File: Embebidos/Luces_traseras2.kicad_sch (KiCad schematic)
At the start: 9 parts, among them J4 RJ45, J5 RJ45, Q1 Q_PMOS_Leds5v, Q2 Q_PMOS_Infrarrojo

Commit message: anotaciones_fix
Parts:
- renumbered J5 to J8, J4 to J9, JT3 to JT1, JT1 to JT2, JT2 to JT3, Q1 to Q4, Q2 to Q5, R2 to R24, R1 to R25
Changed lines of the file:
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@@
   (symbol (lib_id "Connector:RJ45") (at 168.91 93.98 0) (unit 1)
     (in_bom yes) (on_board yes)
-    (property "Reference" "J4" (id 0) (at 170.3578 77.0382 0))
+    (property "Reference" "J9" (id 0) (at 170.3578 77.0382 0))
     (property "Value" "RJ45" (id 1) (at 170.3578 79.3496 0))
     (property "Footprint" "" (id 2) (at 168.91 93.345 90)
@@
   (symbol (lib_id "Connector:Conn_01x03_Male") (at 241.3 64.77 180) (unit 1)
     (in_bom yes) (on_board yes)
-    (property "Reference" "JT1" (id 0) (at 238.5568 71.9074 0))
+    (property "Reference" "JT2" (id 0) (at 238.5568 71.9074 0))
     (property "Value" "8 LEDS RGB Izquierda" (id 1) (at 238.5568 69.596 0))
     (property "Footprint" "" (id 2) (at 241.3 64.77 0)
@@
   (symbol (lib_id "Connector:Conn_01x03_Male") (at 241.3 90.17 180) (unit 1)
     (in_bom yes) (on_board yes)
-    (property "Reference" "JT2" (id 0) (at 238.5568 97.3074 0))
+    (property "Reference" "JT3" (id 0) (at 238.5568 97.3074 0))
     (property "Value" "INFRARROJO SHARP" (id 1) (at 238.5568 94.996 0))
     (property "Footprint" "" (id 2) (at 241.3 90.17 0)
@@
   (symbol (lib_id "Connector:Conn_01x03_Male") (at 240.03 114.3 180) (unit 1)
     (in_bom yes) (on_board yes)
-    (property "Reference" "JT3" (id 0) (at 237.2868 121.4374 0))
+    (property "Reference" "JT1" (id 0) (at 237.2868 121.4374 0))
     (property "Value" "8 LEDS RGB Derecha" (id 1) (at 237.2868 119.126 0))
     (property "Footprint" "" (id 2) (at 240.03 114.3 0)
@@
   (symbol (lib_id "Device:R") (at 203.2 76.2 270) (unit 1)
     (in_bom yes) (on_board yes)
-    (property "Reference" "R1" (id 0) (at 203.2 70.9422 90))
+    (property "Reference" "R25" (id 0) (at 203.2 70.9422 90))
     (property "Value" "470" (id 1) (at 203.2 73.2536 90))
     (property "Footprint" "" (id 2) (at 203.2 74.422 90)
@@
   (symbol (lib_id "Device:R") (at 201.93 107.95 270) (unit 1)
     (in_bom yes) (on_board yes)
-    (property "Reference" "R2" (id 0) (at 201.93 102.6922 90))
+    (property "Reference" "R24" (id 0) (at 201.93 102.6922 90))
     (property "Value" "470" (id 1) (at 201.93 105.0036 90))
     (property "Footprint" "" (id 2) (at 201.93 106.172 90)
@@
   (symbol (lib_id "Connector:RJ45") (at 111.76 91.44 180) (unit 1)
     (in_bom yes) (on_board yes)
-    (property "Reference" "J5" (id 0) (at 120.142 91.5416 0)
+    (property "Reference" "J8" (id 0) (at 120.142 91.5416 0)
       (effects (font (size 1.27 1.27)) (justify right))
     )
@@
   (symbol (lib_id "Device:Q_PMOS_GSD") (at 50.8 116.84 0) (unit 1)
     (in_bom yes) (on_board yes)
-    (property "Reference" "Q1" (id 0) (at 55.9816 115.6716 0)
+    (property "Reference" "Q4" (id 0) (at 55.9816 115.6716 0)
       (effects (font (size 1.27 1.27)) (justify left))
     )
@@
   (symbol (lib_id "Device:Q_PMOS_GSD") (at 62.23 109.22 0) (unit 1)
     (in_bom yes) (on_board yes)
-    (property "Reference" "Q2" (id 0) (at 67.4116 108.0516 0)
+    (property "Reference" "Q5" (id 0) (at 67.4116 108.0516 0)
       (effects (font (size 1.27 1.27)) (justify left))
     )
@@
   (symbol (lib_id "power:+5V") (at 53.34 127 180) (unit 1)
     (in_bom yes) (on_board yes) (fields_autoplaced)
-    (property "Reference" "#PWR?" (id 0) (at 53.34 123.19 0)
+    (property "Reference" "#PWR038" (id 0) (at 53.34 123.19 0)
       (effects (font (size 1.27 1.27)) hide)
     )
@@
   (symbol (lib_id "power:GND") (at 27.94 91.44 270) (unit 1)
     (in_bom yes) (on_board yes) (fields_autoplaced)
-    (property "Reference" "#PWR?" (id 0) (at 21.59 91.44 0)
+    (property "Reference" "#PWR037" (id 0) (at 21.59 91.44 0)
       (effects (font (size 1.27 1.27)) hide)
     )

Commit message: Mosfet Luces
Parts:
- removed Q4: Q_PMOS_Leds5v, symbol Device:Q_PMOS_GSD
- removed Q5: Q_PMOS_Infrarrojo, symbol Device:Q_PMOS_GSD
- added IC?: DMP3056LSD-13, SOIC127P600X175-8N, symbol DMP3056LSD-13:DMP3056LSD-13
- added R? (x2): 1k, symbol Device:R
- added R? (x2): 100k, symbol Device:R
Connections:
- net +5V: now also IC?.1 (S1), IC?.3 (S2), R?.2, R?.2
- net ctr 5v inf: now also R?.1, R?.1
- net ctr 5v leds: now also R?.1, R?.1
- net at J8.2: now also IC?.8 (D1_2)
- net at J8.3: now also IC?.5 (D2_1)
- new net: IC?.2 (G1), R?.2
- new net: IC?.4 (G2), R?.2
- no-connect marks 4 -> 6

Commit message: se agrego el bonito
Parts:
- gave numbers to parts that had none: 5
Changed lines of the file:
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@@
   (symbol (lib_id "Device:R") (at 49.53 137.16 90) (unit 1)
     (in_bom yes) (on_board yes)
-    (property "Reference" "R?" (id 0) (at 49.53 134.62 90))
+    (property "Reference" "R28" (id 0) (at 49.53 134.62 90))
     (property "Value" "1k" (id 1) (at 49.53 137.16 90))
     (property "Footprint" "" (id 2) (at 49.53 138.938 90)
@@
   (symbol (lib_id "Device:R") (at 46.99 115.57 180) (unit 1)
     (in_bom yes) (on_board yes)
-    (property "Reference" "R?" (id 0) (at 44.45 115.57 90))
+    (property "Reference" "R27" (id 0) (at 44.45 115.57 90))
     (property "Value" "100k" (id 1) (at 46.99 115.57 90))
     (property "Footprint" "" (id 2) (at 48.768 115.57 90)
@@
   (symbol (lib_id "power:+5V") (at 46.99 109.22 0) (unit 1)
     (in_bom yes) (on_board yes)
-    (property "Reference" "#PWR?" (id 0) (at 46.99 113.03 0)
+    (property "Reference" "#PWR0104" (id 0) (at 46.99 113.03 0)
       (effects (font (size 1.27 1.27)) hide)
     )
@@
   (symbol (lib_id "Device:R") (at 50.8 127 90) (unit 1)
     (in_bom yes) (on_board yes)
-    (property "Reference" "R?" (id 0) (at 50.8 124.46 90))
+    (property "Reference" "R29" (id 0) (at 50.8 124.46 90))
     (property "Value" "1k" (id 1) (at 50.8 127 90))
     (property "Footprint" "" (id 2) (at 50.8 128.778 90)
@@
   (symbol (lib_id "Device:R") (at 35.56 132.08 180) (unit 1)
     (in_bom yes) (on_board yes)
-    (property "Reference" "R?" (id 0) (at 33.02 132.08 90))
+    (property "Reference" "R26" (id 0) (at 33.02 132.08 90))
     (property "Value" "100k" (id 1) (at 35.56 132.08 90))
     (property "Footprint" "" (id 2) (at 37.338 132.08 90)
@@
   (symbol (lib_id "DMP3056LSD-13:DMP3056LSD-13") (at 57.15 124.46 90) (unit 1)
     (in_bom yes) (on_board yes) (fields_autoplaced)
-    (property "Reference" "IC?" (id 0) (at 68.58 110.4899 90)
+    (property "Reference" "IC2" (id 0) (at 68.58 110.4899 90)
       (effects (font (size 1.27 1.27)) (justify right))
     )
@@
   (symbol (lib_id "power:+5V") (at 35.56 125.73 0) (unit 1)
     (in_bom yes) (on_board yes)
-    (property "Reference" "#PWR?" (id 0) (at 35.56 129.54 0)
+    (property "Reference" "#PWR0105" (id 0) (at 35.56 129.54 0)
       (effects (font (size 1.27 1.27)) hide)
     )

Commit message: transistores traseros
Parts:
- removed IC2: DMP3056LSD-13, SOIC127P600X175-8N, symbol DMP3056LSD-13:DMP3056LSD-13
- removed J9: RJ45, symbol Connector:RJ45
- removed JT1: 8 LEDS RGB Derecha, symbol Connector:Conn_01x03_Male
- removed JT2: 8 LEDS RGB Izquierda, symbol Connector:Conn_01x03_Male
- removed JT3: INFRARROJO SHARP, symbol Connector:Conn_01x03_Male
- removed R26: 100k, symbol Device:R
- removed R29: 1k, symbol Device:R
- added Q?: BSS138, Package_TO_SOT_SMD:SOT-23, symbol Transistor_FET:BSS138
- added Q? (x2): DMP3056LSDQ-13, DMP3056LSD:SOIC127P600X175-8N, symbol DMP3056LSDQ-13:DMP3056LSDQ-13
- added R?: 100k, symbol Device:R
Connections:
- net ctr 5v inf is gone; now on net GND: R27.1
- net +5V: now also Q?.1, Q?.3, R?.2; no longer R27.2
- net Din_der: now also R25.2; no longer J8.1
- net Din_izq: now also R24.2; no longer J8.6
- net GND: now also Q?.2 (S)
- net at R25.1: now also J8.1
- net at R24.1: now also J8.6
- net VCC_LEDS: now reaches J8.2
- net VCC_LEDS: now also Q?.7, Q?.8
- net VCC_INF: now reaches J8.3
- net VCC_INF: now also Q?.5, Q?.6
- net at R28.2: now also R27.2, Q?.1 (G)
- net ctr 5v leds renamed ctr_trasero
- new net: Q?.2, Q?.3 (D), Q?.4, R?.1
- no-connect marks 6 -> 2
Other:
- note added: "2. Control Vcc leds 3. Control Vcc inf"
- moved on the sheet: R24, R25, R27, R28

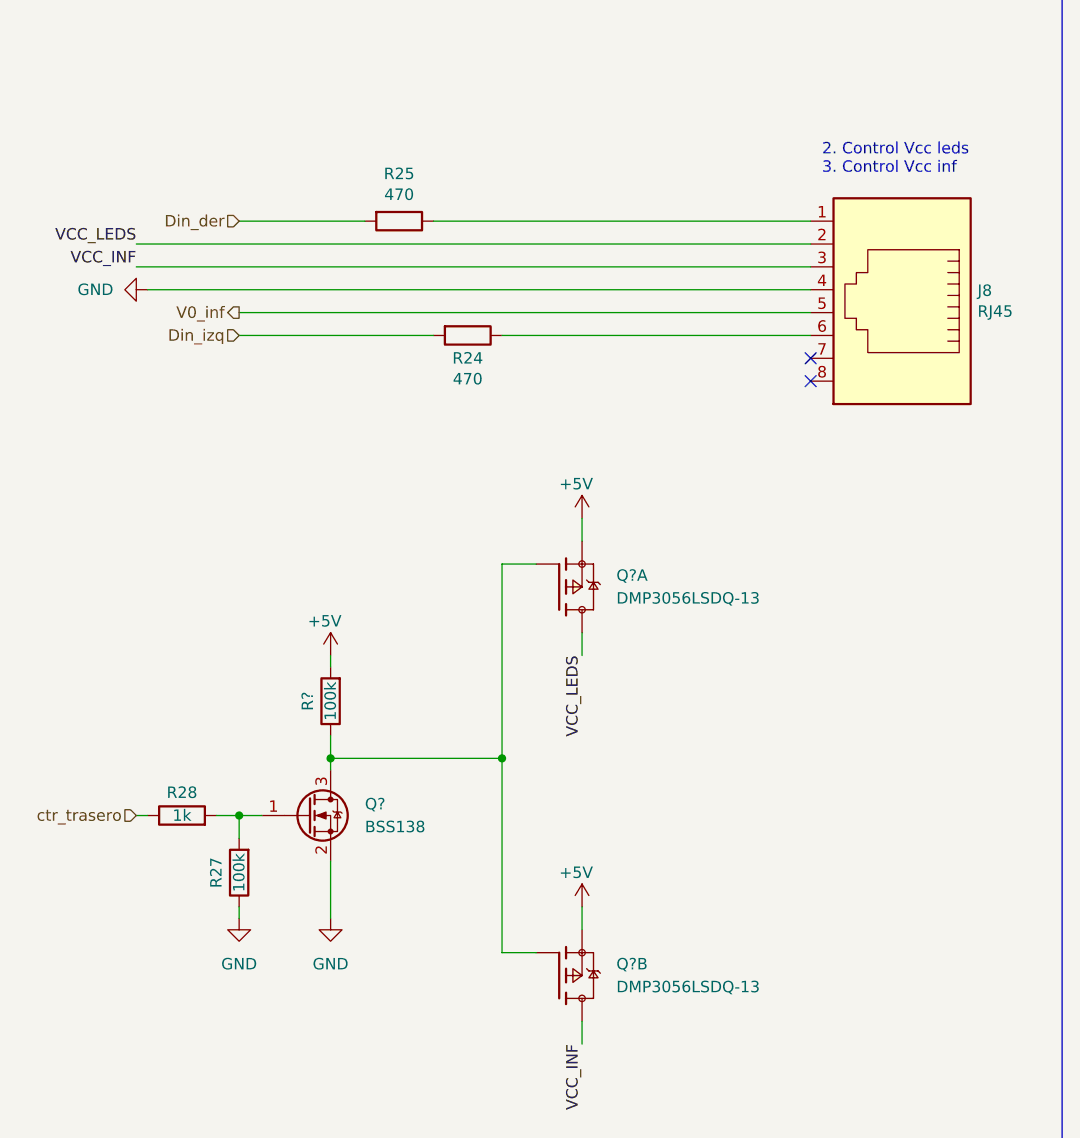
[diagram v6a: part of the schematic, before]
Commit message: Cambio de anotacion y Vcc ldr
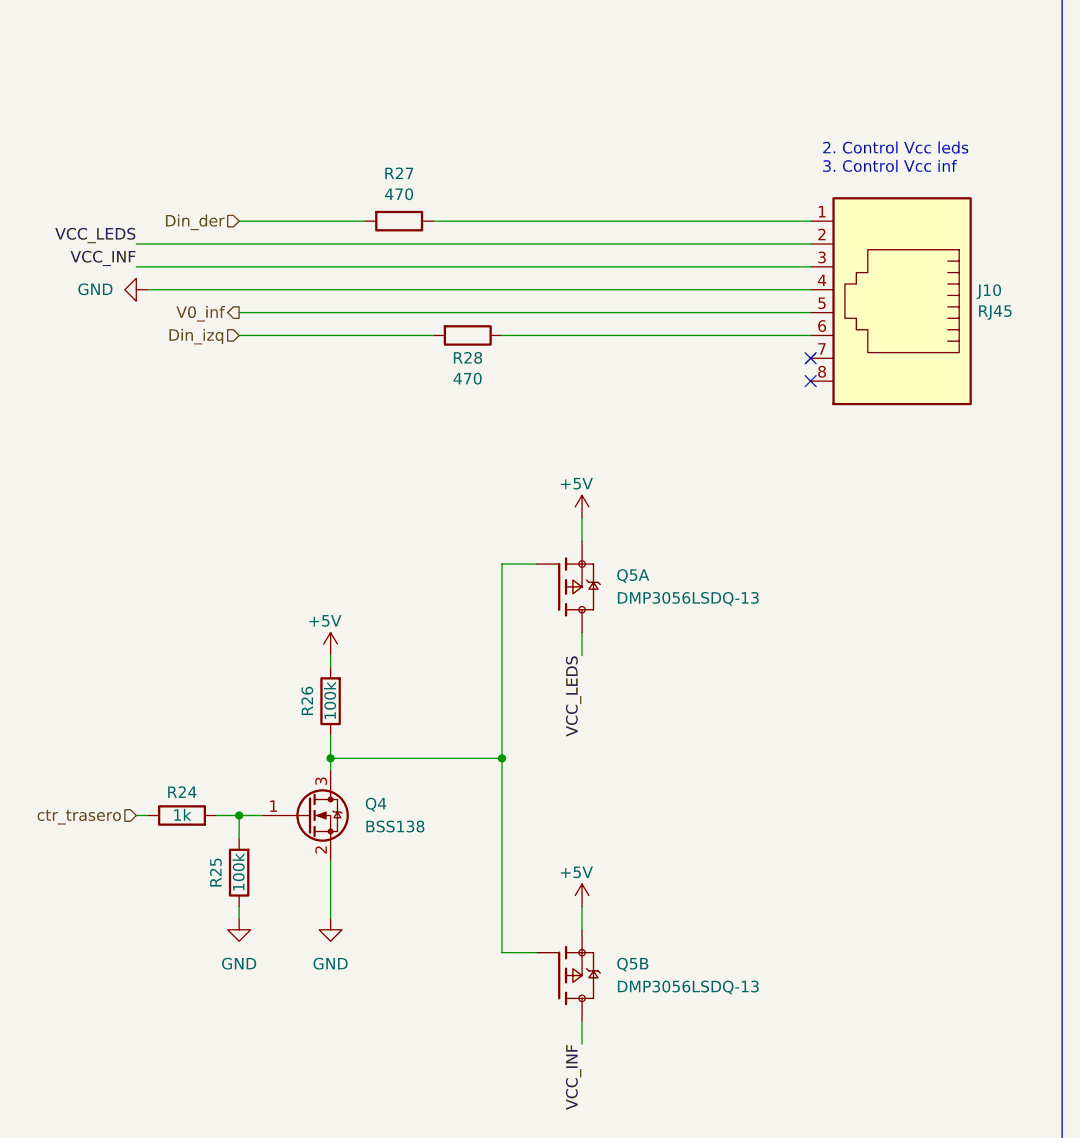
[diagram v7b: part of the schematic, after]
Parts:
- gave numbers to parts that had none: 3
- renumbered J8 to J10, R28 to R24, R27 to R25, R25 to R27, R24 to R28
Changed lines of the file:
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@@
   (symbol (lib_id "Device:R") (at 55.88 83.82 270) (unit 1)
     (in_bom yes) (on_board yes)
-    (property "Reference" "R25" (id 0) (at 55.88 78.5622 90))
+    (property "Reference" "R27" (id 0) (at 55.88 78.5622 90))
     (property "Value" "470" (id 1) (at 55.88 80.8736 90))
     (property "Footprint" "" (id 2) (at 55.88 82.042 90)
@@
   (symbol (lib_id "Device:R") (at 63.5 96.52 270) (unit 1)
     (in_bom yes) (on_board yes)
-    (property "Reference" "R24" (id 0) (at 63.5 99.06 90))
+    (property "Reference" "R28" (id 0) (at 63.5 99.06 90))
     (property "Value" "470" (id 1) (at 63.5 101.3714 90))
     (property "Footprint" "" (id 2) (at 63.5 94.742 90)
@@
   (symbol (lib_id "Connector:RJ45") (at 111.76 91.44 180) (unit 1)
     (in_bom yes) (on_board yes)
-    (property "Reference" "J8" (id 0) (at 120.142 91.5416 0)
+    (property "Reference" "J10" (id 0) (at 120.142 91.5416 0)
       (effects (font (size 1.27 1.27)) (justify right))
     )
@@
   (symbol (lib_id "power:+5V") (at 48.26 132.08 0) (unit 1)
     (in_bom yes) (on_board yes)
-    (property "Reference" "#PWR?" (id 0) (at 48.26 135.89 0)
+    (property "Reference" "#PWR040" (id 0) (at 48.26 135.89 0)
       (effects (font (size 1.27 1.27)) hide)
     )
@@
   (symbol (lib_id "Device:R") (at 31.75 149.86 90) (unit 1)
     (in_bom yes) (on_board yes)
-    (property "Reference" "R28" (id 0) (at 31.75 147.32 90))
+    (property "Reference" "R24" (id 0) (at 31.75 147.32 90))
     (property "Value" "1k" (id 1) (at 31.75 149.86 90))
     (property "Footprint" "" (id 2) (at 31.75 151.638 90)
@@
   (symbol (lib_id "Transistor_FET:BSS138") (at 45.72 149.86 0) (unit 1)
     (in_bom yes) (on_board yes) (fields_autoplaced)
-    (property "Reference" "Q?" (id 0) (at 52.07 148.5899 0)
+    (property "Reference" "Q4" (id 0) (at 52.07 148.5899 0)
       (effects (font (size 1.27 1.27)) (justify left))
     )
@@
   (symbol (lib_id "power:GND") (at 38.1 161.29 0) (unit 1)
     (in_bom yes) (on_board yes)
-    (property "Reference" "#PWR?" (id 0) (at 38.1 167.64 0)
+    (property "Reference" "#PWR039" (id 0) (at 38.1 167.64 0)
       (effects (font (size 1.27 1.27)) hide)
     )
@@
   (symbol (lib_id "Device:R") (at 48.26 137.16 180) (unit 1)
     (in_bom yes) (on_board yes)
-    (property "Reference" "R?" (id 0) (at 45.72 137.16 90))
+    (property "Reference" "R26" (id 0) (at 45.72 137.16 90))
     (property "Value" "100k" (id 1) (at 48.26 137.16 90))
     (property "Footprint" "" (id 2) (at 50.038 137.16 90)
@@
   (symbol (lib_id "power:GND") (at 48.26 161.29 0) (unit 1)
     (in_bom yes) (on_board yes)
-    (property "Reference" "#PWR?" (id 0) (at 48.26 167.64 0)
+    (property "Reference" "#PWR041" (id 0) (at 48.26 167.64 0)
       (effects (font (size 1.27 1.27)) hide)
     )
@@
   (symbol (lib_id "Device:R") (at 38.1 156.21 180) (unit 1)
     (in_bom yes) (on_board yes)
-    (property "Reference" "R27" (id 0) (at 35.56 156.21 90))
+    (property "Reference" "R25" (id 0) (at 35.56 156.21 90))
     (property "Value" "100k" (id 1) (at 38.1 156.21 90))
     (property "Footprint" "" (id 2) (at 39.878 156.21 90)
@@
   (symbol (lib_id "DMP3056LSDQ-13:DMP3056LSDQ-13") (at 73.66 124.46 0) (unit 1)
     (in_bom yes) (on_board yes) (fields_autoplaced)
-    (property "Reference" "Q?" (id 0) (at 80.01 123.1899 0)
+    (property "Reference" "Q5" (id 0) (at 80.01 123.1899 0)
       (effects (font (size 1.27 1.27)) (justify left))
     )
@@
   (symbol (lib_id "power:GND") (at 27.94 91.44 270) (unit 1)
     (in_bom yes) (on_board yes) (fields_autoplaced)
-    (property "Reference" "#PWR037" (id 0) (at 21.59 91.44 0)
+    (property "Reference" "#PWR038" (id 0) (at 21.59 91.44 0)
       (effects (font (size 1.27 1.27)) hide)
     )
@@
   (symbol (lib_id "power:+5V") (at 76.2 160.02 0) (unit 1)
     (in_bom yes) (on_board yes)
-    (property "Reference" "#PWR?" (id 0) (at 76.2 163.83 0)
+    (property "Reference" "#PWR043" (id 0) (at 76.2 163.83 0)
       (effects (font (size 1.27 1.27)) hide)
     )
@@
   (symbol (lib_id "DMP3056LSDQ-13:DMP3056LSDQ-13") (at 73.66 167.64 0) (unit 2)
     (in_bom yes) (on_board yes) (fields_autoplaced)
-    (property "Reference" "Q?" (id 0) (at 80.01 166.3699 0)
+    (property "Reference" "Q5" (id 0) (at 80.01 166.3699 0)
       (effects (font (size 1.27 1.27)) (justify left))
     )
@@
   (symbol (lib_id "power:+5V") (at 76.2 116.84 0) (unit 1)
     (in_bom yes) (on_board yes)
-    (property "Reference" "#PWR0105" (id 0) (at 76.2 120.65 0)
-      (effects (font (size 1.27 1.27)) hide)
-    )
+    (property "Reference" "#PWR042" (id 0) (at 76.2 120.65 0)
+      (effects (font (size 1.27 1.27)) hide)
+    )
